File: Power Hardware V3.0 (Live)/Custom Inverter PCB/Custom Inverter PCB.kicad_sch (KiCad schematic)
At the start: 0 parts

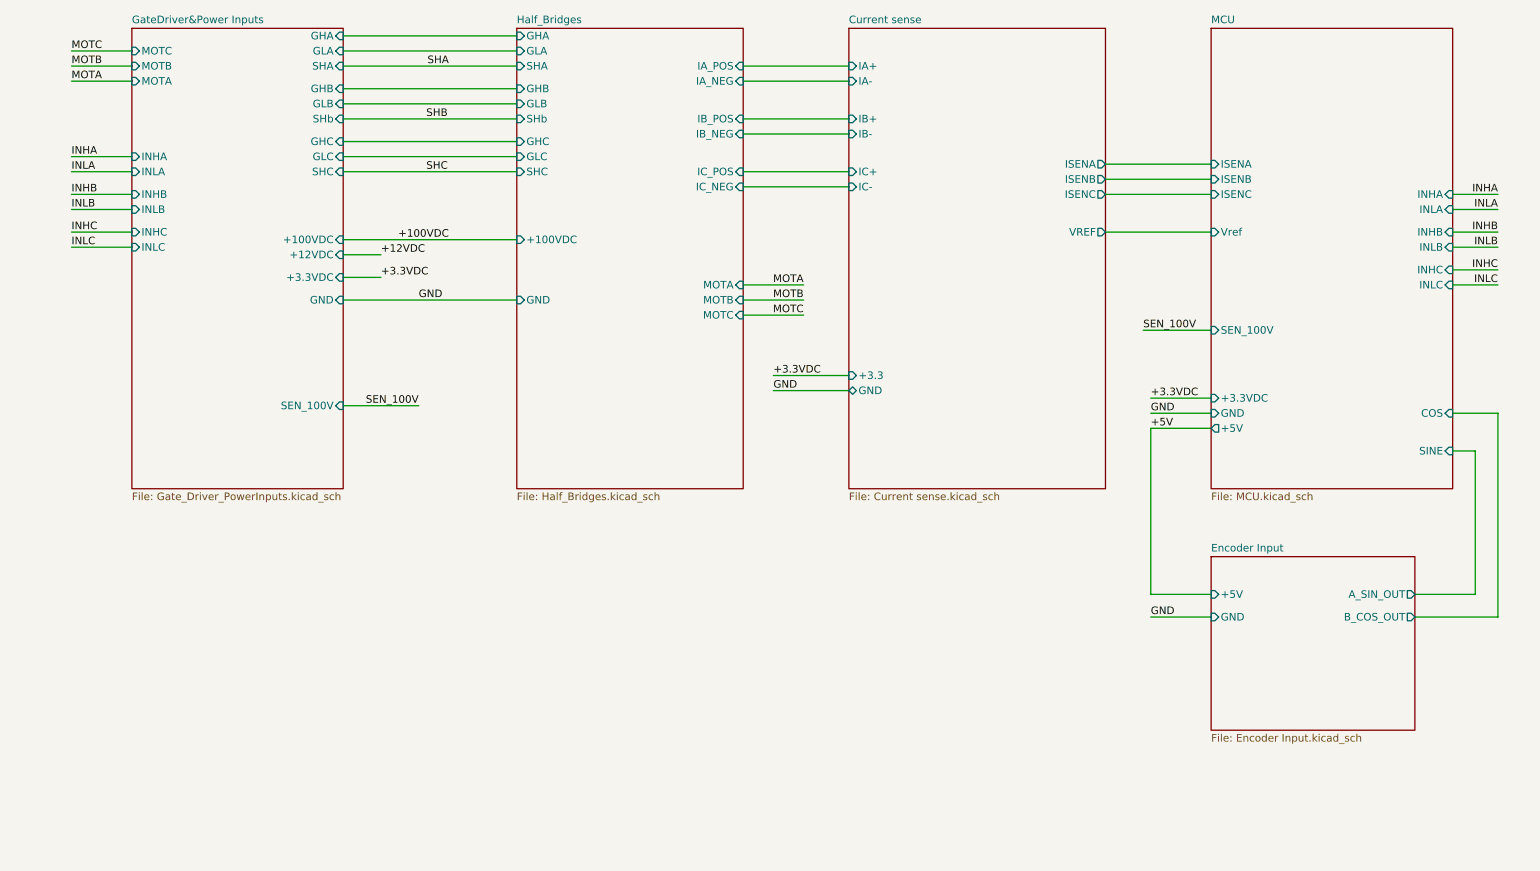
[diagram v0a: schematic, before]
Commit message: Added 100-12 and 12-5 regulators added fan headers
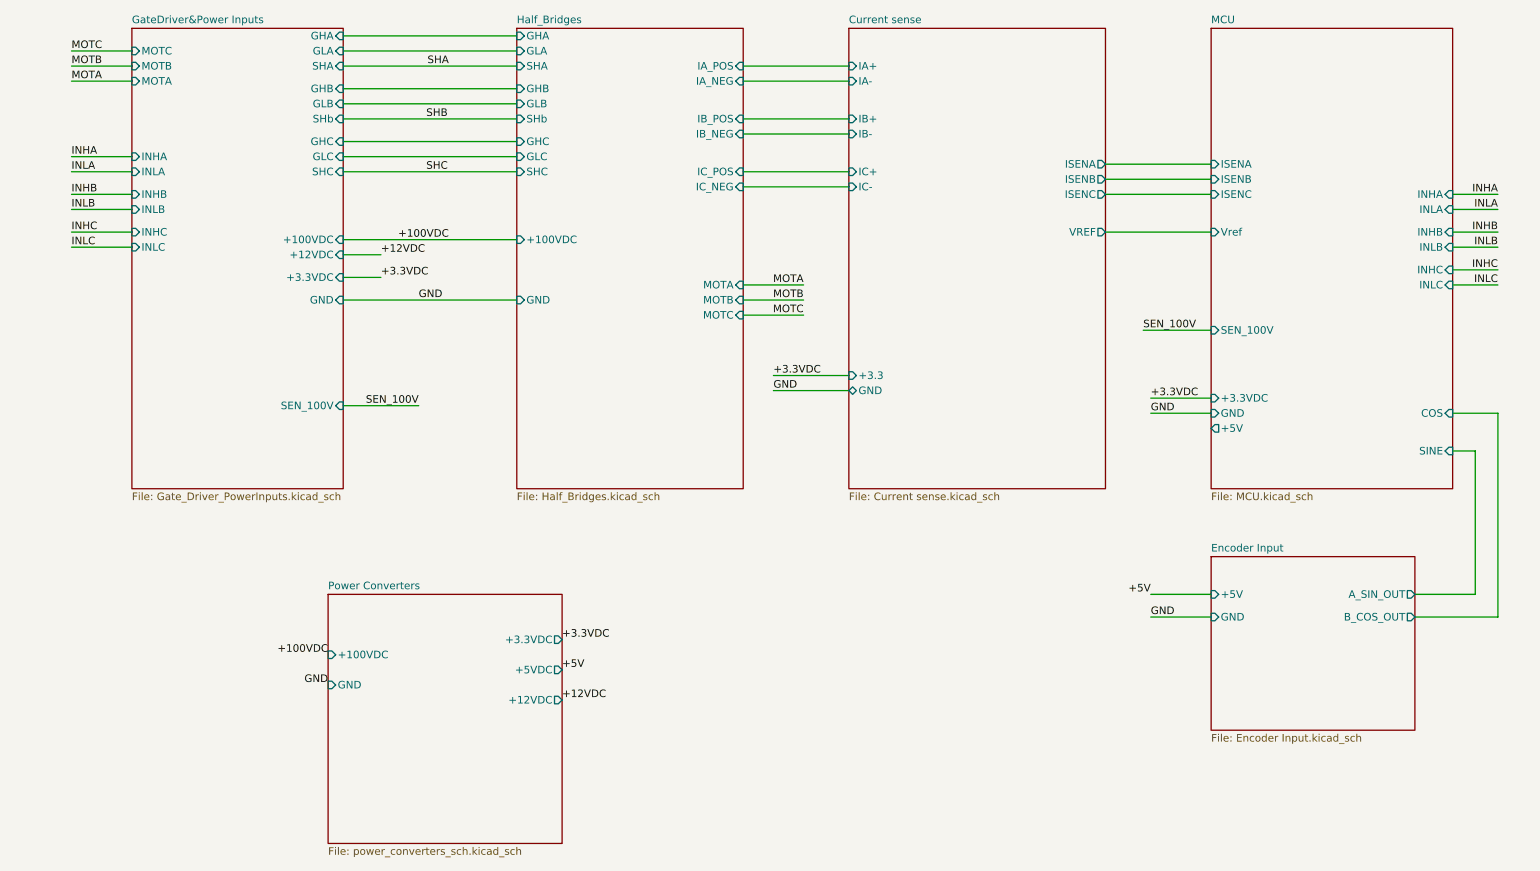
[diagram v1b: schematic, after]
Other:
- added sheet Power Converters (power_converters_sch.kicad_sch)
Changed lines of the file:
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@@
-	(wire
-		(pts
-			(xy 205.74 92.71) (xy 205.74 120.65)
-		)
-		(stroke
-			(width 0)
-			(type default)
-		)
-	)
 	(wire
 		(pts
@@
 		(pts
 			(xy 24.13 53.34) (xy 34.29 53.34)
-		)
-		(stroke
-			(width 0)
-			(type default)
-		)
-	)
-	(wire
-		(pts
-			(xy 215.9 92.71) (xy 205.74 92.71)
 		)
 		(stroke
@@
 		)
 	)
+	(label "+3.3VDC"
+		(at 106.68 128.27 0)
+		(effects
+			(font
+				(size 1.27 1.27)
+			)
+			(justify left bottom)
+		)
+	)
 	(label "MOTB"
 		(at 147.32 71.12 180)
@@
 		)
 	)
+	(label "+12VDC"
+		(at 106.68 138.43 0)
+		(effects
+			(font
+				(size 1.27 1.27)
+			)
+			(justify left bottom)
+		)
+	)
 	(label "INLA"
 		(at 264.16 55.88 180)
@@
 		)
 	)
+	(label "+5V"
+		(at 106.68 133.35 0)
+		(effects
+			(font
+				(size 1.27 1.27)
+			)
+			(justify left bottom)
+		)
+	)
 	(label "SHC"
 		(at 83.82 49.53 0)
@@
 		)
 	)
-	(label "+5V"
-		(at 205.74 92.71 0)
-		(effects
-			(font
-				(size 1.27 1.27)
-			)
-			(justify left bottom)
-		)
-	)
 	(label "SHB"
 		(at 83.82 40.64 0)
@@
 	(label "INHA"
 		(at 264.16 53.34 180)
+		(effects
+			(font
+				(size 1.27 1.27)
+			)
+			(justify right bottom)
+		)
+	)
+	(label "+100VDC"
+		(at 67.31 130.81 180)
+		(effects
+			(font
+				(size 1.27 1.27)
+			)
+			(justify right bottom)
+		)
+	)
+	(label "+5V"
+		(at 205.74 120.65 180)
+		(effects
+			(font
+				(size 1.27 1.27)
+			)
+			(justify right bottom)
+		)
+	)
+	(label "GND"
+		(at 67.31 135.89 180)
 		(effects
 			(font
@@
 				)
 			)
+		)
+	)
+	(sheet
+		(at 67.31 120.65)
+		(size 39.37 41.91)
+		(exclude_from_sim no)
+		(in_bom yes)
+		(on_board yes)
+		(dnp no)
+		(fields_autoplaced yes)
+		(stroke
+			(width 0.1524)
+			(type solid)
+		)
+		(fill
+			(color 0 0 0 0.0000)
+		)
+		(property "Sheetname" "Power Converters"
+			(at 67.31 119.9384 0)
+			(effects
+				(font
+					(size 1.27 1.27)
+				)
+				(justify left bottom)
+			)
+		)
+		(property "Sheetfile" "power_converters_sch.kicad_sch"
+			(at 67.31 163.1446 0)
+			(effects
+				(font
+					(size 1.27 1.27)
+				)
+				(justify left top)
+			)
+		)
+		(pin "+3.3VDC" output
+			(at 106.68 128.27 0)
+			(effects
+				(font
+					(size 1.27 1.27)
+				)
+				(justify right)
+			)
+		)
+		(pin "+5VDC" output
+			(at 106.68 133.35 0)
+			(effects
+				(font
+					(size 1.27 1.27)
+				)
+				(justify right)
+			)
+		)
+		(pin "+12VDC" output
+			(at 106.68 138.43 0)
+			(effects
+				(font
+					(size 1.27 1.27)
+				)
+				(justify right)
+			)
+		)
+		(pin "+100VDC" input
+			(at 67.31 130.81 180)
+			(effects
+				(font
+					(size 1.27 1.27)
+				)
+				(justify left)
+			)
+		)
+		(pin "GND" input
+			(at 67.31 135.89 180)
+			(effects
+				(font
+					(size 1.27 1.27)
+				)
+				(justify left)
+			)
+		)
+		(instances
+			(project "Custom Inverter PCB"
+				(path "/3e1046b6-e265-4cdd-8404-c358cfc105fe"
+					(page "7")
+				)
+			)

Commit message: Fixes
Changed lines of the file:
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@@
+	(wire
+		(pts
+			(xy 82.55 129.54) (xy 73.66 129.54)
+		)
+		(stroke
+			(width 0)
+			(type default)
+		)
+	)
 	(wire
 		(pts
@@
 	(wire
 		(pts
+			(xy 82.55 124.46) (xy 73.66 124.46)
+		)
+		(stroke
+			(width 0)
+			(type default)
+		)
+	)
+	(wire
+		(pts
 			(xy 76.2 63.5) (xy 69.85 63.5)
 		)
@@
 	(wire
 		(pts
+			(xy 205.74 92.71) (xy 215.9 92.71)
+		)
+		(stroke
+			(width 0)
+			(type default)
+		)
+	)
+	(wire
+		(pts
 			(xy 137.16 49.53) (xy 154.94 49.53)
 		)
@@
 	(wire
 		(pts
+			(xy 24.13 132.08) (xy 34.29 132.08)
+		)
+		(stroke
+			(width 0)
+			(type default)
+		)
+	)
+	(wire
+		(pts
 			(xy 69.85 49.53) (xy 99.06 49.53)
 		)
@@
 	(wire
 		(pts
+			(xy 82.55 134.62) (xy 73.66 134.62)
+		)
+		(stroke
+			(width 0)
+			(type default)
+		)
+	)
+	(wire
+		(pts
 			(xy 137.16 40.64) (xy 154.94 40.64)
 		)
@@
 		(pts
 			(xy 137.16 31.75) (xy 154.94 31.75)
+		)
+		(stroke
+			(width 0)
+			(type default)
+		)
+	)
+	(wire
+		(pts
+			(xy 24.13 127) (xy 34.29 127)
 		)
 		(stroke
@@
 	)
 	(label "+3.3VDC"
-		(at 106.68 128.27 0)
+		(at 82.55 124.46 0)
 		(effects
 			(font
@@
 	)
 	(label "+12VDC"
-		(at 106.68 138.43 0)
+		(at 82.55 134.62 0)
 		(effects
 			(font
@@
 		)
 	)
+	(label "+5V"
+		(at 205.74 92.71 0)
+		(effects
+			(font
+				(size 1.27 1.27)
+			)
+			(justify left bottom)
+		)
+	)
 	(label "+100VDC"
 		(at 87.63 60.96 180)
@@
 	)
 	(label "+5V"
-		(at 106.68 133.35 0)
+		(at 82.55 129.54 0)
 		(effects
 			(font
@@
 	)
 	(label "+100VDC"
-		(at 67.31 130.81 180)
+		(at 24.13 127 180)
 		(effects
 			(font
@@
 	)
 	(label "+5V"
-		(at 205.74 120.65 180)
-		(effects
-			(font
-				(size 1.27 1.27)
-			)
-			(justify right bottom)
+		(at 205.74 120.65 0)
+		(effects
+			(font
+				(size 1.27 1.27)
+			)
+			(justify left bottom)
 		)
 	)
 	(label "GND"
-		(at 67.31 135.89 180)
+		(at 24.13 132.08 180)
 		(effects
 			(font
@@
 	)
 	(sheet
-		(at 67.31 120.65)
+		(at 34.29 116.84)
 		(size 39.37 41.91)
 		(exclude_from_sim no)
@@
 		)
 		(property "Sheetname" "Power Converters"
-			(at 67.31 119.9384 0)
+			(at 34.29 116.1284 0)
 			(effects
 				(font
@@
 		)
 		(property "Sheetfile" "power_converters_sch.kicad_sch"
-			(at 67.31 163.1446 0)
+			(at 34.29 159.3346 0)
 			(effects
 				(font
@@
 		)
 		(pin "+3.3VDC" output
-			(at 106.68 128.27 0)
+			(at 73.66 124.46 0)
 			(effects
 				(font
@@
 		)
 		(pin "+5VDC" output
-			(at 106.68 133.35 0)
+			(at 73.66 129.54 0)
 			(effects
 				(font
@@
 		)
 		(pin "+12VDC" output
-			(at 106.68 138.43 0)
+			(at 73.66 134.62 0)
 			(effects
 				(font
@@
 		)
 		(pin "+100VDC" input
-			(at 67.31 130.81 180)
+			(at 34.29 127 180)
 			(effects
 				(font
@@
 		)
 		(pin "GND" input
-			(at 67.31 135.89 180)
-			(effects
-				(font
+			(at 34.29 132.08 180)
+			(effects
+				(font

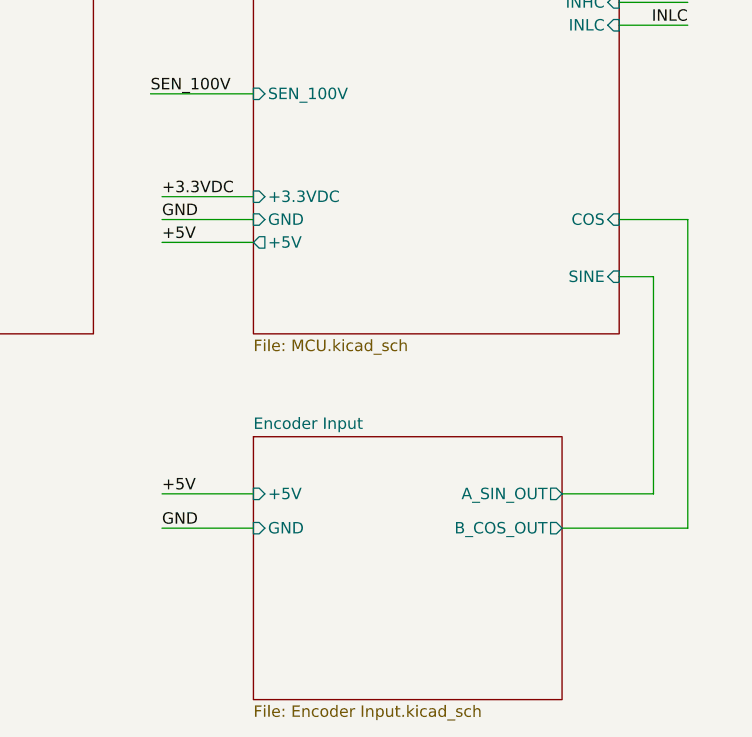
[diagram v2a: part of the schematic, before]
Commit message: PCB V3 changes
-HV outputs and inputs changed to screw terminals for lugs
- Fuses changes to 50A
- ADC pin for temp sense along with the temp sensing circuit
- Added more pins to motor encoder term for temp sense
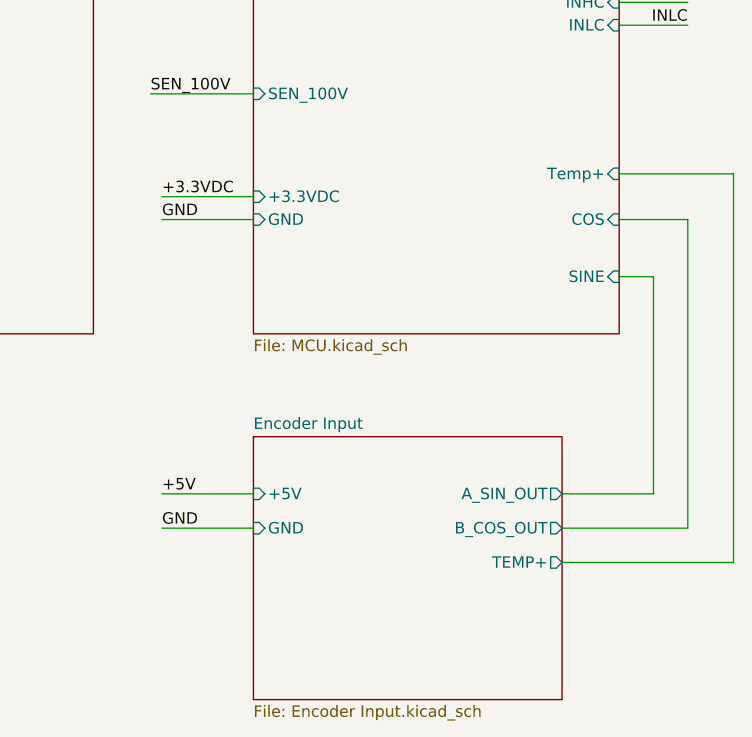
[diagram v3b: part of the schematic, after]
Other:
- sheet Encoder Input ports: added TEMP+; removed none
- sheet MCU ports: added Temp+; removed +5V
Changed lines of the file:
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@@
+	(wire
+		(pts
+			(xy 269.24 128.27) (xy 250.19 128.27)
+		)
+		(stroke
+			(width 0)
+			(type default)
+		)
+	)
 	(wire
 		(pts
@@
 	(wire
 		(pts
+			(xy 256.54 85.09) (xy 269.24 85.09)
+		)
+		(stroke
+			(width 0)
+			(type default)
+		)
+	)
+	(wire
+		(pts
 			(xy 82.55 88.9) (xy 69.85 88.9)
 		)
@@
 	(wire
 		(pts
+			(xy 269.24 85.09) (xy 269.24 128.27)
+		)
+		(stroke
+			(width 0)
+			(type default)
+		)
+	)
+	(wire
+		(pts
 			(xy 69.85 31.75) (xy 99.06 31.75)
 		)
@@
 		(pts
 			(xy 256.54 90.17) (xy 264.16 90.17)
-		)
-		(stroke
-			(width 0)
-			(type default)
-		)
-	)
-	(wire
-		(pts
-			(xy 205.74 92.71) (xy 215.9 92.71)
 		)
 		(stroke
@@
 	(label "MOTB"
 		(at 24.13 31.75 0)
-		(effects
-			(font
-				(size 1.27 1.27)
-			)
-			(justify left bottom)
-		)
-	)
-	(label "+5V"
-		(at 205.74 92.71 0)
 		(effects
 			(font
@@
 			)
 		)
-		(pin "+5V" output
-			(at 215.9 92.71 180)
-			(effects
-				(font
-					(size 1.27 1.27)
-				)
-				(justify left)
-			)
-		)
 		(pin "COS" input
 			(at 256.54 90.17 0)
@@
 		(pin "SINE" input
 			(at 256.54 96.52 0)
+			(effects
+				(font
+					(size 1.27 1.27)
+				)
+				(justify right)
+			)
+		)
+		(pin "Temp+" input
+			(at 256.54 85.09 0)
 			(effects
 				(font
@@
 			)
 		)
+		(pin "TEMP+" output
+			(at 250.19 128.27 0)
+			(effects
+				(font
+					(size 1.27 1.27)
+				)
+				(justify right)
+			)
+		)

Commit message: PCB layout
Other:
- sheet Current sense ports: added OCD1_A, OCD1_B, OCD1_C, OCD2_A, OCD2_B, OCD2_C; removed none
- sheet MCU ports: added OCD1_A, OCD1_B, OCD1_C, OCD2_A, OCD2_B, OCD2_C; removed none
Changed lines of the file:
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@@
+	(wire
+		(pts
+			(xy 198.12 46.99) (xy 215.9 46.99)
+		)
+		(stroke
+			(width 0)
+			(type default)
+		)
+	)
 	(wire
 		(pts
@@
 	(wire
 		(pts
+			(xy 198.12 44.45) (xy 215.9 44.45)
+		)
+		(stroke
+			(width 0)
+			(type default)
+		)
+	)
+	(wire
+		(pts
 			(xy 76.2 67.31) (xy 69.85 67.31)
 		)
@@
 	(wire
 		(pts
+			(xy 198.12 40.64) (xy 215.9 40.64)
+		)
+		(stroke
+			(width 0)
+			(type default)
+		)
+	)
+	(wire
+		(pts
 			(xy 250.19 124.46) (xy 264.16 124.46)
 		)
@@
 	(wire
 		(pts
-			(xy 198.12 53.34) (xy 215.9 53.34)
-		)
-		(stroke
-			(width 0)
-			(type default)
-		)
-	)
-	(wire
-		(pts
-			(xy 198.12 59.69) (xy 215.9 59.69)
+			(xy 198.12 60.96) (xy 215.9 60.96)
+		)
+		(stroke
+			(width 0)
+			(type default)
+		)
+	)
+	(wire
+		(pts
+			(xy 198.12 67.31) (xy 215.9 67.31)
 		)
 		(stroke
@@
 	(wire
 		(pts
-			(xy 198.12 50.8) (xy 215.9 50.8)
+			(xy 198.12 58.42) (xy 215.9 58.42)
 		)
 		(stroke
@@
 	(wire
 		(pts
-			(xy 198.12 48.26) (xy 215.9 48.26)
+			(xy 198.12 55.88) (xy 215.9 55.88)
 		)
 		(stroke
@@
 	(wire
 		(pts
+			(xy 198.12 31.75) (xy 215.9 31.75)
+		)
+		(stroke
+			(width 0)
+			(type default)
+		)
+	)
+	(wire
+		(pts
+			(xy 198.12 34.29) (xy 215.9 34.29)
+		)
+		(stroke
+			(width 0)
+			(type default)
+		)
+	)
+	(wire
+		(pts
 			(xy 24.13 127) (xy 34.29 127)
 		)
@@
 		(pts
 			(xy 264.16 53.34) (xy 256.54 53.34)
+		)
+		(stroke
+			(width 0)
+			(type default)
+		)
+	)
+	(wire
+		(pts
+			(xy 198.12 38.1) (xy 215.9 38.1)
 		)
 		(stroke
@@
 		)
 		(pin "ISENC" input
-			(at 215.9 53.34 180)
+			(at 215.9 60.96 180)
 			(effects
 				(font
@@
 		)
 		(pin "ISENB" input
-			(at 215.9 50.8 180)
+			(at 215.9 58.42 180)
 			(effects
 				(font
@@
 		)
 		(pin "ISENA" input
-			(at 215.9 48.26 180)
+			(at 215.9 55.88 180)
 			(effects
 				(font
@@
 		)
 		(pin "Vref" input
-			(at 215.9 59.69 180)
+			(at 215.9 67.31 180)
 			(effects
 				(font
@@
 				)
 				(justify right)
+			)
+		)
+		(pin "OCD2_A" input
+			(at 215.9 34.29 180)
+			(effects
+				(font
+					(size 1.27 1.27)
+				)
+				(justify left)
+			)
+		)
+		(pin "OCD1_A" input
+			(at 215.9 31.75 180)
+			(effects
+				(font
+					(size 1.27 1.27)
+				)
+				(justify left)
+			)
+		)
+		(pin "OCD1_B" input
+			(at 215.9 38.1 180)
+			(effects
+				(font
+					(size 1.27 1.27)
+				)
+				(justify left)
+			)
+		)
+		(pin "OCD1_C" input
+			(at 215.9 44.45 180)
+			(effects
+				(font
+					(size 1.27 1.27)
+				)
+				(justify left)
+			)
+		)
+		(pin "OCD2_C" input
+			(at 215.9 46.99 180)
+			(effects
+				(font
+					(size 1.27 1.27)
+				)
+				(justify left)
+			)
+		)
+		(pin "OCD2_B" input
+			(at 215.9 40.64 180)
+			(effects
+				(font
+					(size 1.27 1.27)
+				)
+				(justify left)
 			)
 		)
@@
 		)
 		(pin "ISENB" output
-			(at 198.12 50.8 0)
+			(at 198.12 58.42 0)
 			(effects
 				(font
@@
 		)
 		(pin "ISENA" output
-			(at 198.12 48.26 0)
+			(at 198.12 55.88 0)
 			(effects
 				(font
@@
 		)
 		(pin "ISENC" output
-			(at 198.12 53.34 0)
+			(at 198.12 60.96 0)
 			(effects
 				(font
@@
 		)
 		(pin "VREF" output
-			(at 198.12 59.69 0)
-			(effects
-				(font
+			(at 198.12 67.31 0)
+			(effects
+				(font
+					(size 1.27 1.27)
+				)
+				(justify right)
+			)
+		)
+		(pin "OCD2_A" output
+			(at 198.12 34.29 0)
+			(effects
+				(font
+					(size 1.27 1.27)
+				)
+				(justify right)
+			)
+		)
+		(pin "OCD1_B" output
+			(at 198.12 38.1 0)
+			(effects
+				(font
+					(size 1.27 1.27)
+				)
+				(justify right)
+			)
+		)
+		(pin "OCD2_B" output
+			(at 198.12 40.64 0)
+			(effects
+				(font
+					(size 1.27 1.27)
+				)
+				(justify right)
+			)
+		)
+		(pin "OCD1_A" output
+			(at 198.12 31.75 0)
+			(effects
+				(font
+					(size 1.27 1.27)
+				)
+				(justify right)
+			)
+		)
+		(pin "OCD1_C" output
+			(at 198.12 44.45 0)
+			(effects
+				(font
+					(size 1.27 1.27)
+				)
+				(justify right)
+			)
+		)
+		(pin "OCD2_C" output
+			(at 198.12 46.99 0)
+			(effects
+				(font
